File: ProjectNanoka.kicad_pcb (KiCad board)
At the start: 2 copper layers, 66 x 70 mm, 41 parts, among them K1 2-1462038-1, P1 ST_20A, Q1 2N3904BU, Q2 2N3904BU, U1 TLV70033DDCR, U2 NC7WZ16P6X, U3 PS1440P02BT

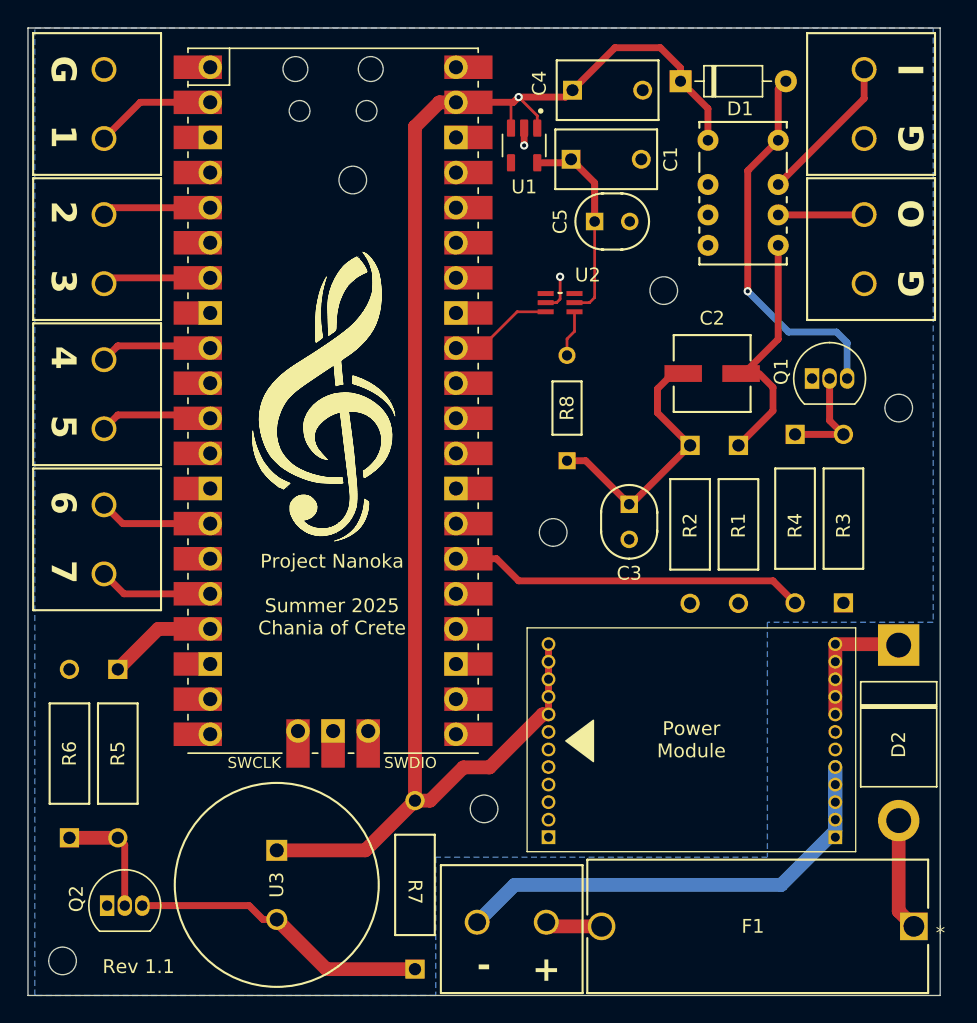
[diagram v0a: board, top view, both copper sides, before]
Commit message: Modified decoupling problem at layout
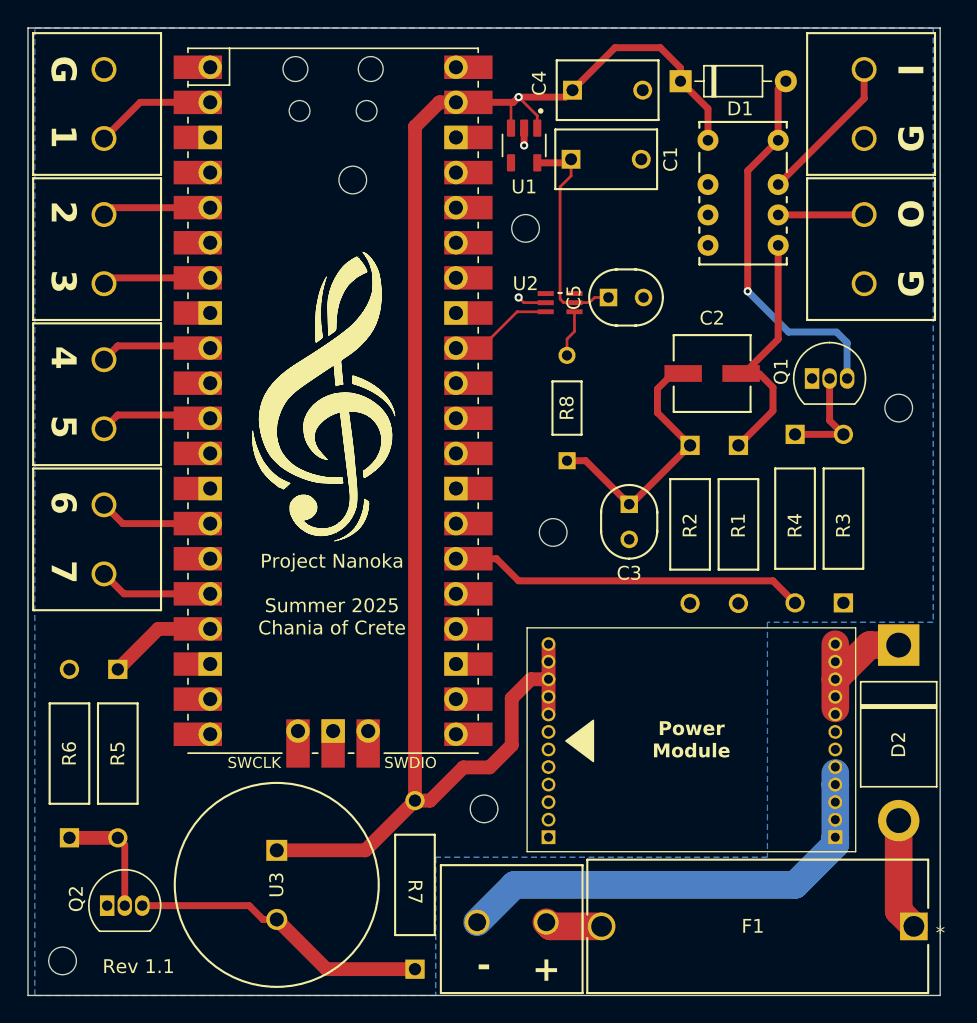
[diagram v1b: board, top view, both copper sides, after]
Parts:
- moved REF** 11.0 mm to (235.5, 56.5)
- moved C5 5.59 mm to (241.5, 61.5)
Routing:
- net +5V: track 111.3 -> 114.4 mm
- net 3.3AS: track 14.9 -> 16.8 mm
- net Net-(H2-Pin_1): track 38.3 -> 39.8 mm
- net Net-(D2-K): track 9.70 -> 10.4 mm
- net GNDPWR: track 4.02 -> 3.37 mm
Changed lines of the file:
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@@
 			(drillshape 0)
 			(scaleselection 1)
-			(outputdirectory "../../../../Desktop/PCBs/Nanoka/v2/")
+			(outputdirectory "GBRs/")
 		)
 	)
@@
 		(at 238 61.873)
 		(property "Reference" "U2"
-			(at 2 -2 0)
+			(at -2.5 -1.373 0)
 			(layer "F.SilkS")
 			(effects
@@
 	(footprint "Footprints:CAP_C320_KEM"
 		(layer "F.Cu")
-		(at 240.5 56)
+		(at 241.5 61.5)
 		(tags "C320C104K5R5TA ")
 		(property "Reference" "C5"
@@
 	(footprint "Footprints:MountingHole_2mm"
 		(layer "F.Cu")
-		(at 245.5 61)
+		(at 235.5 56.5)
 		(descr "Mounting Hole 2mm, no annular")
 		(tags "mounting hole 2mm no annular")
@@
 			(font
 				(size 1 1)
-				(thickness 0.1)
+				(thickness 0.2)
+				(bold yes)
 			)
 		)
@@
 	)
 	(segment
-		(start 238 61.6158)
-		(end 238 60)
-		(width 0.2)
-		(layer "F.Cu")
-		(net 2)
-	)
-	(segment
 		(start 236.9586 61.873)
-		(end 237.7428 61.873)
+		(end 235.373 61.873)
 		(width 0.2)
 		(layer "F.Cu")
@@
 	)
 	(segment
-		(start 237.7428 61.873)
-		(end 238 61.6158)
+		(start 235.373 61.873)
+		(end 235 61.5)
 		(width 0.2)
 		(layer "F.Cu")
@@
 	)
 	(via
-		(at 238 60)
+		(at 235 61.5)
 		(size 0.6)
 		(drill 0.3)
@@
 	)
 	(segment
+		(start 234.5 93.896529)
+		(end 234.5 90.5)
+		(width 1)
+		(layer "F.Cu")
+		(net 6)
+	)
+	(segment
+		(start 235.8775 89.1225)
+		(end 237.1625 89.1225)
+		(width 1)
+		(layer "F.Cu")
+		(net 6)
+	)
+	(segment
 		(start 223.904 101.5)
 		(end 227.5 97.904)
@@
 	)
 	(segment
-		(start 237.1625 86.5825)
-		(end 237.1625 91.6625)
-		(width 0.5)
-		(layer "F.Cu")
-		(net 6)
-	)
-	(segment
 		(start 236.34815 48.34815)
 		(end 236.34815 49.245)
@@
 	)
 	(segment
-		(start 237.1625 91.6625)
-		(end 236.734029 91.6625)
-		(width 1)
-		(layer "F.Cu")
-		(net 6)
-	)
-	(segment
 		(start 238.39815 47)
 		(end 238.89815 46.5)
@@
 	)
 	(segment
+		(start 237.1625 86.5825)
+		(end 237.1625 91.6625)
+		(width 1)
+		(layer "F.Cu")
+		(net 6)
+	)
+	(segment
 		(start 235 47)
 		(end 234.44815 47.55185)
@@
 	)
 	(segment
-		(start 236.734029 91.6625)
-		(end 232.896529 95.5)
+		(start 227.5 97.904)
+		(end 227.5 49.142919)
 		(width 1)
 		(layer "F.Cu")
@@
 	)
 	(segment
-		(start 227.5 97.904)
-		(end 227.5 49.142919)
+		(start 234.5 90.5)
+		(end 235.8775 89.1225)
 		(width 1)
 		(layer "F.Cu")
@@
 	)
 	(segment
+		(start 232.896529 95.5)
+		(end 234.5 93.896529)
+		(width 1)
+		(layer "F.Cu")
+		(net 6)
+	)
+	(segment
 		(start 234.62 47.38)
 		(end 235 47)
@@
 	)
 	(segment
+		(start 239.0414 61.873)
+		(end 238.2572 61.873)
+		(width 0.2)
+		(layer "F.Cu")
+		(net 15)
+	)
+	(segment
 		(start 236.34815 51.755)
 		(end 238.5413 51.755)
@@
 	)
 	(segment
-		(start 240.5 53.2037)
-		(end 238.7963 51.5)
-		(width 0.5)
+		(start 238.2572 61.873)
+		(end 238 61.6158)
+		(width 0.2)
 		(layer "F.Cu")
 		(net 15)
@@
 	(segment
 		(start 240.5 61.5)
-		(end 240.5 56)
+		(end 241.5 61.5)
 		(width 0.2)
 		(layer "F.Cu")
@@
 	)
 	(segment
-		(start 240.5 56)
-		(end 240.5 53.2037)
-		(width 0.5)
+		(start 238 53.5)
+		(end 238.7963 52.7037)
+		(width 0.2)
 		(layer "F.Cu")
 		(net 15)
@@
 	)
 	(segment
+		(start 238 61.6158)
+		(end 238 53.5)
+		(width 0.2)
+		(layer "F.Cu")
+		(net 15)
+	)
+	(segment
 		(start 238.5413 51.755)
 		(end 238.7963 51.5)
@@
 	)
 	(segment
+		(start 238.7963 52.7037)
+		(end 238.7963 51.5)
+		(width 0.2)
+		(layer "F.Cu")
+		(net 15)
+	)
+	(segment
 		(start 253.78 46.405)
 		(end 254.335 45.85)
@@
 	)
 	(segment
-		(start 262.5 99.35)
-		(end 262.5 105.9)
-		(width 1)
+		(start 262.5 105.9)
+		(end 263.6 107)
+		(width 2)
 		(layer "F.Cu")
 		(net 30)
 	)
 	(segment
-		(start 262.5 105.9)
-		(end 263.6 107)
-		(width 1)
+		(start 262.5 99.35)
+		(end 262.5 105.9)
+		(width 2)
 		(layer "F.Cu")
 		(net 30)
@@
 	)
 	(segment
-		(start 257.9125 86.5825)
-		(end 257.9125 91.6625)
-		(width 1)
+		(start 260.385 86.65)
+		(end 257.9125 89.1225)
+		(width 2)
 		(layer "F.Cu")
 		(net 32)
@@
 	(segment
 		(start 257.9125 86.5825)
-		(end 262.4325 86.5825)
-		(width 1)
+		(end 257.9125 91.2315)
+		(width 2)
+		(layer "F.Cu")
+		(net 32)
+	)
+	(segment
+		(start 262.5 86.65)
+		(end 260.385 86.65)
+		(width 2)
 		(layer "F.Cu")
 		(net 32)
@@
 	)
 	(segment
-		(start 241 107)
-		(end 237.3 107)
-		(width 1)
+		(start 237.3 107)
+		(end 237 106.7)
+		(width 2)
 		(layer "F.Cu")
 		(net 33)
 	)
 	(segment
-		(start 237.3 107)
-		(end 237 106.7)
-		(width 1)
+		(start 241 107)
+		(end 237.3 107)
+		(width 2)
 		(layer "F.Cu")
 		(net 33)
@@
 	)
 	(segment
-		(start 254 104)
-		(end 234.7 104)
-		(width 1)
+		(start 234.7 104)
+		(end 255 104)
+		(width 2)
 		(layer "B.Cu")
 		(net 35)
 	)
 	(segment
-		(start 257.9125 100.0875)
-		(end 254 104)
+		(start 257.9125 95.4725)
+		(end 257.9125 100.5525)
 		(width 1)
 		(layer "B.Cu")
@@
 	)
 	(segment
-		(start 257.9125 95.4725)
+		(start 257.9125 96.7425)
 		(end 257.9125 100.5525)
-		(width 1)
+		(width 2)
 		(layer "B.Cu")
 		(net 35)
 	)
 	(segment
-		(start 234.7 104)
-		(end 232 106.7)
-		(width 1)
+		(start 255 104)
+		(end 257.9125 101.0875)
+		(width 2)
+		(layer "B.Cu")
+		(net 35)
+	)
+	(segment
+		(start 257.9125 101.0875)
+		(end 257.9125 100.5525)
+		(width 2)
+		(layer "B.Cu")
+		(net 35)
+	)
+	(segment
+		(start 232 106.7)
+		(end 234.7 104)
+		(width 2)
 		(layer "B.Cu")
 		(net 35)
@@
 	(segment
 		(start 257.9125 96.7425)
-		(end 257.9125 100.0875)
-		(width 1)
+		(end 257.9125 95.9035)
+		(width 2)
 		(layer "B.Cu")
 		(net 35)
